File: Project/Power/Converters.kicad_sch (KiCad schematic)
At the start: 7 parts, among them U1 AP63203WU

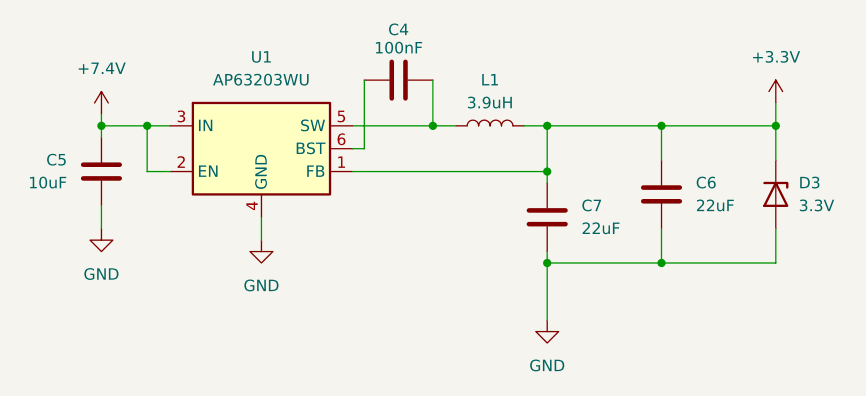
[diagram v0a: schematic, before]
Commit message: Add high-side power switch with LM74502
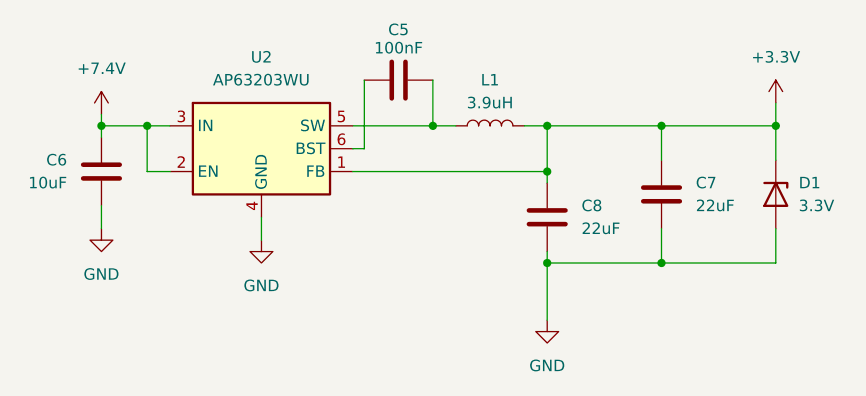
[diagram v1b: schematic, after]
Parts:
- renumbered C4 to C5, C5 to C6, C6 to C7, C7 to C8, D3 to D1, U1 to U2
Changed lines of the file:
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@@
 		(on_board yes)
 		(dnp no)
-		(property "Reference" "C6"
+		(property "Reference" "C7"
 			(at 116.84 44.4499 0)
 			(effects
@@
 			(project "XuLabPower"
 				(path "/71bb14ae-b730-4d22-a41d-cf68989dae2d/39e94aee-ccd8-45cb-a26b-136997d4dd4d"
-					(reference "C6")
+					(reference "C7")
 					(unit 1)
 				)
@@
 		(dnp no)
 		(fields_autoplaced yes)
-		(property "Reference" "#PWR05"
+		(property "Reference" "#PWR09"
 			(at 125.73 39.37 0)
 			(effects
@@
 			(project "XuLabPower"
 				(path "/71bb14ae-b730-4d22-a41d-cf68989dae2d/39e94aee-ccd8-45cb-a26b-136997d4dd4d"
-					(reference "#PWR05")
+					(reference "#PWR09")
 					(unit 1)
 				)
@@
 		(dnp no)
 		(fields_autoplaced yes)
-		(property "Reference" "U1"
+		(property "Reference" "U2"
 			(at 68.58 30.48 0)
 			(effects
@@
 			(project "XuLabPower"
 				(path "/71bb14ae-b730-4d22-a41d-cf68989dae2d/39e94aee-ccd8-45cb-a26b-136997d4dd4d"
-					(reference "U1")
+					(reference "U2")
 					(unit 1)
 				)
@@
 		(dnp no)
 		(fields_autoplaced yes)
-		(property "Reference" "#PWR07"
+		(property "Reference" "#PWR011"
 			(at 50.8 55.88 0)
 			(effects
@@
 			(project "XuLabPower"
 				(path "/71bb14ae-b730-4d22-a41d-cf68989dae2d/39e94aee-ccd8-45cb-a26b-136997d4dd4d"
-					(reference "#PWR07")
+					(reference "#PWR011")
 					(unit 1)
 				)
@@
 		(dnp no)
 		(fields_autoplaced yes)
-		(property "Reference" "#PWR09"
+		(property "Reference" "#PWR013"
 			(at 100.33 66.04 0)
 			(effects
@@
 			(project "XuLabPower"
 				(path "/71bb14ae-b730-4d22-a41d-cf68989dae2d/39e94aee-ccd8-45cb-a26b-136997d4dd4d"
-					(reference "#PWR09")
+					(reference "#PWR013")
 					(unit 1)
 				)
@@
 		(on_board yes)
 		(dnp no)
-		(property "Reference" "C5"
+		(property "Reference" "C6"
 			(at 46.99 41.9099 0)
 			(effects
@@
 			(project "XuLabPower"
 				(path "/71bb14ae-b730-4d22-a41d-cf68989dae2d/39e94aee-ccd8-45cb-a26b-136997d4dd4d"
-					(reference "C5")
+					(reference "C6")
 					(unit 1)
 				)
@@
 		(on_board yes)
 		(dnp no)
-		(property "Reference" "C4"
+		(property "Reference" "C5"
 			(at 83.82 27.432 90)
 			(effects
@@
 			(project "XuLabPower"
 				(path "/71bb14ae-b730-4d22-a41d-cf68989dae2d/39e94aee-ccd8-45cb-a26b-136997d4dd4d"
-					(reference "C4")
+					(reference "C5")
 					(unit 1)
 				)
@@
 		(dnp no)
 		(fields_autoplaced yes)
-		(property "Reference" "D3"
+		(property "Reference" "D1"
 			(at 128.27 44.4499 90)
 			(effects
@@
 			(project "XuLabPower"
 				(path "/71bb14ae-b730-4d22-a41d-cf68989dae2d/39e94aee-ccd8-45cb-a26b-136997d4dd4d"
-					(reference "D3")
+					(reference "D1")
 					(unit 1)
 				)
@@
 		(dnp no)
 		(fields_autoplaced yes)
-		(property "Reference" "#PWR06"
+		(property "Reference" "#PWR010"
 			(at 50.8 40.64 0)
 			(effects
@@
 			(project "XuLabPower"
 				(path "/71bb14ae-b730-4d22-a41d-cf68989dae2d/39e94aee-ccd8-45cb-a26b-136997d4dd4d"
-					(reference "#PWR06")
+					(reference "#PWR010")
 					(unit 1)
 				)
@@
 		(dnp no)
 		(fields_autoplaced yes)
-		(property "Reference" "#PWR08"
+		(property "Reference" "#PWR012"
 			(at 68.58 57.15 0)
 			(effects
@@
 			(project "XuLabPower"
 				(path "/71bb14ae-b730-4d22-a41d-cf68989dae2d/39e94aee-ccd8-45cb-a26b-136997d4dd4d"
-					(reference "#PWR08")
+					(reference "#PWR012")
 					(unit 1)
 				)
@@
 		(on_board yes)
 		(dnp no)
-		(property "Reference" "C7"
+		(property "Reference" "C8"
 			(at 104.14 46.9899 0)
 			(effects
@@
 			(project "XuLabPower"
 				(path "/71bb14ae-b730-4d22-a41d-cf68989dae2d/39e94aee-ccd8-45cb-a26b-136997d4dd4d"
-					(reference "C7")
-					(unit 1)
-				)
+					(reference "C8")
+					(unit 1)
+				)

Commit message: Add indicator LEDs to the batteries
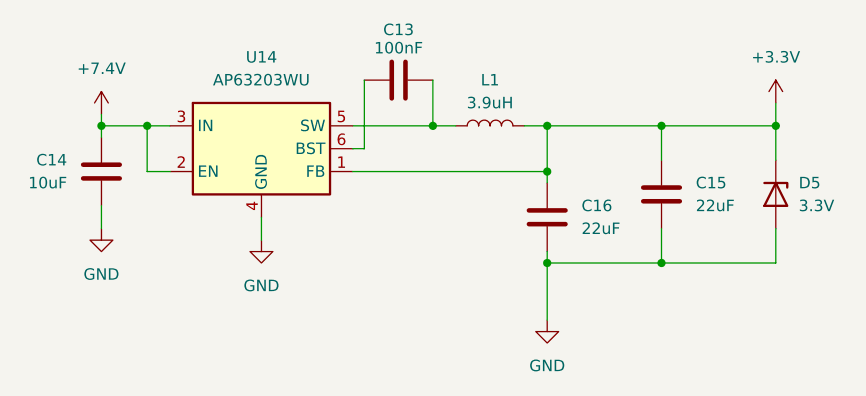
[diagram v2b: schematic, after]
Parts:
- renumbered C5 to C13, C6 to C14, C7 to C15, C8 to C16, D1 to D5, U2 to U14
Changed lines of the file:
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@@
 		(on_board yes)
 		(dnp no)
-		(property "Reference" "C7"
+		(property "Reference" "C15"
 			(at 116.84 44.4499 0)
 			(effects
@@
 			(project "XuLabPower"
 				(path "/71bb14ae-b730-4d22-a41d-cf68989dae2d/39e94aee-ccd8-45cb-a26b-136997d4dd4d"
-					(reference "C7")
+					(reference "C15")
 					(unit 1)
 				)
@@
 		(dnp no)
 		(fields_autoplaced yes)
-		(property "Reference" "#PWR09"
+		(property "Reference" "#PWR060"
 			(at 125.73 39.37 0)
 			(effects
@@
 			(project "XuLabPower"
 				(path "/71bb14ae-b730-4d22-a41d-cf68989dae2d/39e94aee-ccd8-45cb-a26b-136997d4dd4d"
-					(reference "#PWR09")
+					(reference "#PWR060")
 					(unit 1)
 				)
@@
 		(dnp no)
 		(fields_autoplaced yes)
-		(property "Reference" "U2"
+		(property "Reference" "U14"
 			(at 68.58 30.48 0)
 			(effects
@@
 			(project "XuLabPower"
 				(path "/71bb14ae-b730-4d22-a41d-cf68989dae2d/39e94aee-ccd8-45cb-a26b-136997d4dd4d"
-					(reference "U2")
+					(reference "U14")
 					(unit 1)
 				)
@@
 		(dnp no)
 		(fields_autoplaced yes)
-		(property "Reference" "#PWR011"
+		(property "Reference" "#PWR062"
 			(at 50.8 55.88 0)
 			(effects
@@
 			(project "XuLabPower"
 				(path "/71bb14ae-b730-4d22-a41d-cf68989dae2d/39e94aee-ccd8-45cb-a26b-136997d4dd4d"
-					(reference "#PWR011")
+					(reference "#PWR062")
 					(unit 1)
 				)
@@
 		(dnp no)
 		(fields_autoplaced yes)
-		(property "Reference" "#PWR013"
+		(property "Reference" "#PWR064"
 			(at 100.33 66.04 0)
 			(effects
@@
 			(project "XuLabPower"
 				(path "/71bb14ae-b730-4d22-a41d-cf68989dae2d/39e94aee-ccd8-45cb-a26b-136997d4dd4d"
-					(reference "#PWR013")
+					(reference "#PWR064")
 					(unit 1)
 				)
@@
 		(on_board yes)
 		(dnp no)
-		(property "Reference" "C6"
+		(property "Reference" "C14"
 			(at 46.99 41.9099 0)
 			(effects
@@
 			(project "XuLabPower"
 				(path "/71bb14ae-b730-4d22-a41d-cf68989dae2d/39e94aee-ccd8-45cb-a26b-136997d4dd4d"
-					(reference "C6")
+					(reference "C14")
 					(unit 1)
 				)
@@
 		(on_board yes)
 		(dnp no)
-		(property "Reference" "C5"
+		(property "Reference" "C13"
 			(at 83.82 27.432 90)
 			(effects
@@
 			(project "XuLabPower"
 				(path "/71bb14ae-b730-4d22-a41d-cf68989dae2d/39e94aee-ccd8-45cb-a26b-136997d4dd4d"
-					(reference "C5")
+					(reference "C13")
 					(unit 1)
 				)
@@
 		(dnp no)
 		(fields_autoplaced yes)
-		(property "Reference" "D1"
+		(property "Reference" "D5"
 			(at 128.27 44.4499 90)
 			(effects
@@
 			(project "XuLabPower"
 				(path "/71bb14ae-b730-4d22-a41d-cf68989dae2d/39e94aee-ccd8-45cb-a26b-136997d4dd4d"
-					(reference "D1")
+					(reference "D5")
 					(unit 1)
 				)
@@
 		(dnp no)
 		(fields_autoplaced yes)
-		(property "Reference" "#PWR010"
+		(property "Reference" "#PWR061"
 			(at 50.8 40.64 0)
 			(effects
@@
 			(project "XuLabPower"
 				(path "/71bb14ae-b730-4d22-a41d-cf68989dae2d/39e94aee-ccd8-45cb-a26b-136997d4dd4d"
-					(reference "#PWR010")
+					(reference "#PWR061")
 					(unit 1)
 				)
@@
 		(dnp no)
 		(fields_autoplaced yes)
-		(property "Reference" "#PWR012"
+		(property "Reference" "#PWR063"
 			(at 68.58 57.15 0)
 			(effects
@@
 			(project "XuLabPower"
 				(path "/71bb14ae-b730-4d22-a41d-cf68989dae2d/39e94aee-ccd8-45cb-a26b-136997d4dd4d"
-					(reference "#PWR012")
+					(reference "#PWR063")
 					(unit 1)
 				)
@@
 		(on_board yes)
 		(dnp no)
-		(property "Reference" "C8"
+		(property "Reference" "C16"
 			(at 104.14 46.9899 0)
 			(effects
@@
 			(project "XuLabPower"
 				(path "/71bb14ae-b730-4d22-a41d-cf68989dae2d/39e94aee-ccd8-45cb-a26b-136997d4dd4d"
-					(reference "C8")
-					(unit 1)
-				)
+					(reference "C16")
+					(unit 1)
+				)

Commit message: Add STM32L422KBTx microcontroller
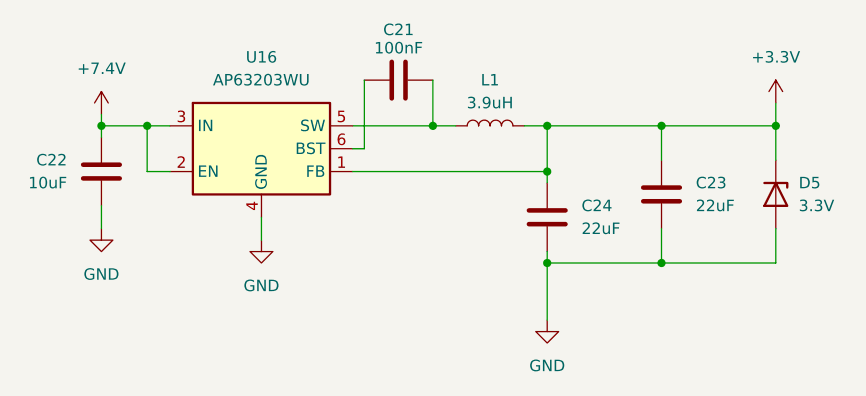
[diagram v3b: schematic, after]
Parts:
- renumbered C13 to C21, C14 to C22, C15 to C23, C16 to C24, U14 to U16
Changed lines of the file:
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@@
 		(on_board yes)
 		(dnp no)
-		(property "Reference" "C15"
+		(property "Reference" "C23"
 			(at 116.84 44.4499 0)
 			(effects
@@
 			(project "XuLabPower"
 				(path "/71bb14ae-b730-4d22-a41d-cf68989dae2d/39e94aee-ccd8-45cb-a26b-136997d4dd4d"
-					(reference "C15")
+					(reference "C23")
 					(unit 1)
 				)
@@
 		(dnp no)
 		(fields_autoplaced yes)
-		(property "Reference" "#PWR060"
+		(property "Reference" "#PWR076"
 			(at 125.73 39.37 0)
 			(effects
@@
 			(project "XuLabPower"
 				(path "/71bb14ae-b730-4d22-a41d-cf68989dae2d/39e94aee-ccd8-45cb-a26b-136997d4dd4d"
-					(reference "#PWR060")
+					(reference "#PWR076")
 					(unit 1)
 				)
@@
 		(dnp no)
 		(fields_autoplaced yes)
-		(property "Reference" "U14"
+		(property "Reference" "U16"
 			(at 68.58 30.48 0)
 			(effects
@@
 			(project "XuLabPower"
 				(path "/71bb14ae-b730-4d22-a41d-cf68989dae2d/39e94aee-ccd8-45cb-a26b-136997d4dd4d"
-					(reference "U14")
+					(reference "U16")
 					(unit 1)
 				)
@@
 		(dnp no)
 		(fields_autoplaced yes)
-		(property "Reference" "#PWR062"
+		(property "Reference" "#PWR078"
 			(at 50.8 55.88 0)
 			(effects
@@
 			(project "XuLabPower"
 				(path "/71bb14ae-b730-4d22-a41d-cf68989dae2d/39e94aee-ccd8-45cb-a26b-136997d4dd4d"
-					(reference "#PWR062")
+					(reference "#PWR078")
 					(unit 1)
 				)
@@
 		(dnp no)
 		(fields_autoplaced yes)
-		(property "Reference" "#PWR064"
+		(property "Reference" "#PWR080"
 			(at 100.33 66.04 0)
 			(effects
@@
 			(project "XuLabPower"
 				(path "/71bb14ae-b730-4d22-a41d-cf68989dae2d/39e94aee-ccd8-45cb-a26b-136997d4dd4d"
-					(reference "#PWR064")
+					(reference "#PWR080")
 					(unit 1)
 				)
@@
 		(on_board yes)
 		(dnp no)
-		(property "Reference" "C14"
+		(property "Reference" "C22"
 			(at 46.99 41.9099 0)
 			(effects
@@
 			(project "XuLabPower"
 				(path "/71bb14ae-b730-4d22-a41d-cf68989dae2d/39e94aee-ccd8-45cb-a26b-136997d4dd4d"
-					(reference "C14")
+					(reference "C22")
 					(unit 1)
 				)
@@
 		(on_board yes)
 		(dnp no)
-		(property "Reference" "C13"
+		(property "Reference" "C21"
 			(at 83.82 27.432 90)
 			(effects
@@
 			(project "XuLabPower"
 				(path "/71bb14ae-b730-4d22-a41d-cf68989dae2d/39e94aee-ccd8-45cb-a26b-136997d4dd4d"
-					(reference "C13")
+					(reference "C21")
 					(unit 1)
 				)
@@
 		(dnp no)
 		(fields_autoplaced yes)
-		(property "Reference" "#PWR061"
+		(property "Reference" "#PWR077"
 			(at 50.8 40.64 0)
 			(effects
@@
 			(project "XuLabPower"
 				(path "/71bb14ae-b730-4d22-a41d-cf68989dae2d/39e94aee-ccd8-45cb-a26b-136997d4dd4d"
-					(reference "#PWR061")
+					(reference "#PWR077")
 					(unit 1)
 				)
@@
 		(dnp no)
 		(fields_autoplaced yes)
-		(property "Reference" "#PWR063"
+		(property "Reference" "#PWR079"
 			(at 68.58 57.15 0)
 			(effects
@@
 			(project "XuLabPower"
 				(path "/71bb14ae-b730-4d22-a41d-cf68989dae2d/39e94aee-ccd8-45cb-a26b-136997d4dd4d"
-					(reference "#PWR063")
+					(reference "#PWR079")
 					(unit 1)
 				)
@@
 		(on_board yes)
 		(dnp no)
-		(property "Reference" "C16"
+		(property "Reference" "C24"
 			(at 104.14 46.9899 0)
 			(effects
@@
 			(project "XuLabPower"
 				(path "/71bb14ae-b730-4d22-a41d-cf68989dae2d/39e94aee-ccd8-45cb-a26b-136997d4dd4d"
-					(reference "C16")
-					(unit 1)
-				)
+					(reference "C24")
+					(unit 1)
+				)

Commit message: Make microcontroller always-on
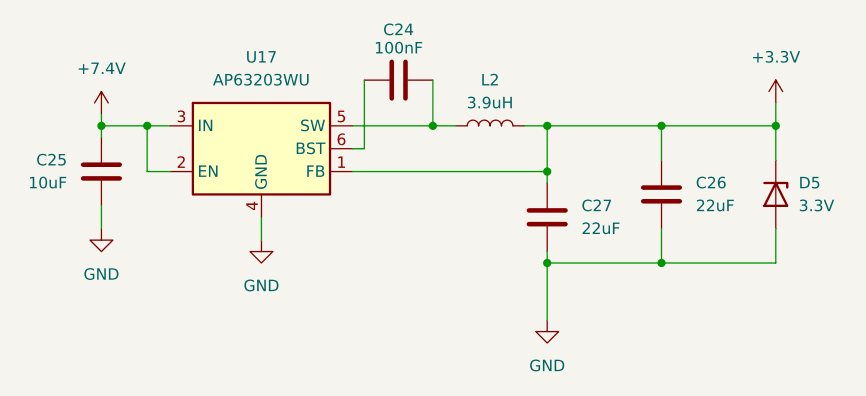
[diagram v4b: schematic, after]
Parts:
- renumbered C21 to C24, C22 to C25, C23 to C26, C24 to C27, L1 to L2, U16 to U17
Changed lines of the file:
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@@
 		(on_board yes)
 		(dnp no)
-		(property "Reference" "C23"
+		(property "Reference" "C26"
 			(at 116.84 44.4499 0)
 			(effects
@@
 			(project "XuLabPower"
 				(path "/71bb14ae-b730-4d22-a41d-cf68989dae2d/39e94aee-ccd8-45cb-a26b-136997d4dd4d"
-					(reference "C23")
+					(reference "C26")
 					(unit 1)
 				)
@@
 		(dnp no)
 		(fields_autoplaced yes)
-		(property "Reference" "#PWR076"
+		(property "Reference" "#PWR078"
 			(at 125.73 39.37 0)
 			(effects
@@
 			(project "XuLabPower"
 				(path "/71bb14ae-b730-4d22-a41d-cf68989dae2d/39e94aee-ccd8-45cb-a26b-136997d4dd4d"
-					(reference "#PWR076")
+					(reference "#PWR078")
 					(unit 1)
 				)
@@
 		(dnp no)
 		(fields_autoplaced yes)
-		(property "Reference" "U16"
+		(property "Reference" "U17"
 			(at 68.58 30.48 0)
 			(effects
@@
 			(project "XuLabPower"
 				(path "/71bb14ae-b730-4d22-a41d-cf68989dae2d/39e94aee-ccd8-45cb-a26b-136997d4dd4d"
-					(reference "U16")
+					(reference "U17")
 					(unit 1)
 				)
@@
 		(dnp no)
 		(fields_autoplaced yes)
-		(property "Reference" "#PWR078"
+		(property "Reference" "#PWR080"
 			(at 50.8 55.88 0)
 			(effects
@@
 			(project "XuLabPower"
 				(path "/71bb14ae-b730-4d22-a41d-cf68989dae2d/39e94aee-ccd8-45cb-a26b-136997d4dd4d"
-					(reference "#PWR078")
+					(reference "#PWR080")
 					(unit 1)
 				)
@@
 		(dnp no)
 		(fields_autoplaced yes)
-		(property "Reference" "#PWR080"
+		(property "Reference" "#PWR082"
 			(at 100.33 66.04 0)
 			(effects
@@
 			(project "XuLabPower"
 				(path "/71bb14ae-b730-4d22-a41d-cf68989dae2d/39e94aee-ccd8-45cb-a26b-136997d4dd4d"
-					(reference "#PWR080")
+					(reference "#PWR082")
 					(unit 1)
 				)
@@
 		(on_board yes)
 		(dnp no)
-		(property "Reference" "C22"
+		(property "Reference" "C25"
 			(at 46.99 41.9099 0)
 			(effects
@@
 			(project "XuLabPower"
 				(path "/71bb14ae-b730-4d22-a41d-cf68989dae2d/39e94aee-ccd8-45cb-a26b-136997d4dd4d"
-					(reference "C22")
+					(reference "C25")
 					(unit 1)
 				)
@@
 		(on_board yes)
 		(dnp no)
-		(property "Reference" "C21"
+		(property "Reference" "C24"
 			(at 83.82 27.432 90)
 			(effects
@@
 			(project "XuLabPower"
 				(path "/71bb14ae-b730-4d22-a41d-cf68989dae2d/39e94aee-ccd8-45cb-a26b-136997d4dd4d"
-					(reference "C21")
+					(reference "C24")
 					(unit 1)
 				)
@@
 		(dnp no)
 		(fields_autoplaced yes)
-		(property "Reference" "#PWR077"
+		(property "Reference" "#PWR079"
 			(at 50.8 40.64 0)
 			(effects
@@
 			(project "XuLabPower"
 				(path "/71bb14ae-b730-4d22-a41d-cf68989dae2d/39e94aee-ccd8-45cb-a26b-136997d4dd4d"
-					(reference "#PWR077")
+					(reference "#PWR079")
 					(unit 1)
 				)
@@
 		(dnp no)
 		(fields_autoplaced yes)
-		(property "Reference" "L1"
+		(property "Reference" "L2"
 			(at 93.98 33.02 90)
 			(effects
@@
 			(project "XuLabPower"
 				(path "/71bb14ae-b730-4d22-a41d-cf68989dae2d/39e94aee-ccd8-45cb-a26b-136997d4dd4d"
-					(reference "L1")
+					(reference "L2")
 					(unit 1)
 				)
@@
 		(dnp no)
 		(fields_autoplaced yes)
-		(property "Reference" "#PWR079"
+		(property "Reference" "#PWR081"
 			(at 68.58 57.15 0)
 			(effects
@@
 			(project "XuLabPower"
 				(path "/71bb14ae-b730-4d22-a41d-cf68989dae2d/39e94aee-ccd8-45cb-a26b-136997d4dd4d"
-					(reference "#PWR079")
+					(reference "#PWR081")
 					(unit 1)
 				)
@@
 		(on_board yes)
 		(dnp no)
-		(property "Reference" "C24"
+		(property "Reference" "C27"
 			(at 104.14 46.9899 0)
 			(effects
@@
 			(project "XuLabPower"
 				(path "/71bb14ae-b730-4d22-a41d-cf68989dae2d/39e94aee-ccd8-45cb-a26b-136997d4dd4d"
-					(reference "C24")
-					(unit 1)
-				)
+					(reference "C27")
+					(unit 1)
+				)

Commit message: Add SPI and I2C connectors for microcontroller
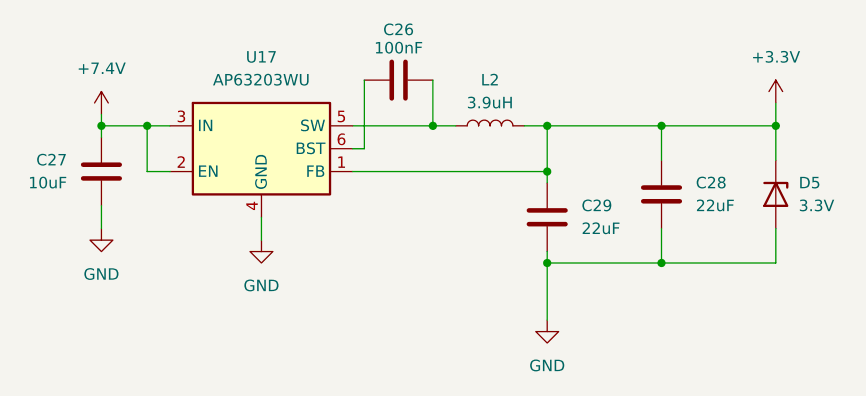
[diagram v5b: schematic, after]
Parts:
- renumbered C24 to C26, C25 to C27, C26 to C28, C27 to C29
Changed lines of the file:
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@@
 		(on_board yes)
 		(dnp no)
-		(property "Reference" "C26"
+		(property "Reference" "C28"
 			(at 116.84 44.4499 0)
 			(effects
@@
 			(project "XuLabPower"
 				(path "/71bb14ae-b730-4d22-a41d-cf68989dae2d/39e94aee-ccd8-45cb-a26b-136997d4dd4d"
-					(reference "C26")
+					(reference "C28")
 					(unit 1)
 				)
@@
 		(dnp no)
 		(fields_autoplaced yes)
-		(property "Reference" "#PWR078"
+		(property "Reference" "#PWR086"
 			(at 125.73 39.37 0)
 			(effects
@@
 			(project "XuLabPower"
 				(path "/71bb14ae-b730-4d22-a41d-cf68989dae2d/39e94aee-ccd8-45cb-a26b-136997d4dd4d"
-					(reference "#PWR078")
+					(reference "#PWR086")
 					(unit 1)
 				)
@@
 		(dnp no)
 		(fields_autoplaced yes)
-		(property "Reference" "#PWR080"
+		(property "Reference" "#PWR088"
 			(at 50.8 55.88 0)
 			(effects
@@
 			(project "XuLabPower"
 				(path "/71bb14ae-b730-4d22-a41d-cf68989dae2d/39e94aee-ccd8-45cb-a26b-136997d4dd4d"
-					(reference "#PWR080")
+					(reference "#PWR088")
 					(unit 1)
 				)
@@
 		(dnp no)
 		(fields_autoplaced yes)
-		(property "Reference" "#PWR082"
+		(property "Reference" "#PWR090"
 			(at 100.33 66.04 0)
 			(effects
@@
 			(project "XuLabPower"
 				(path "/71bb14ae-b730-4d22-a41d-cf68989dae2d/39e94aee-ccd8-45cb-a26b-136997d4dd4d"
-					(reference "#PWR082")
+					(reference "#PWR090")
 					(unit 1)
 				)
@@
 		(on_board yes)
 		(dnp no)
-		(property "Reference" "C25"
+		(property "Reference" "C27"
 			(at 46.99 41.9099 0)
 			(effects
@@
 			(project "XuLabPower"
 				(path "/71bb14ae-b730-4d22-a41d-cf68989dae2d/39e94aee-ccd8-45cb-a26b-136997d4dd4d"
-					(reference "C25")
+					(reference "C27")
 					(unit 1)
 				)
@@
 		(on_board yes)
 		(dnp no)
-		(property "Reference" "C24"
+		(property "Reference" "C26"
 			(at 83.82 27.432 90)
 			(effects
@@
 			(project "XuLabPower"
 				(path "/71bb14ae-b730-4d22-a41d-cf68989dae2d/39e94aee-ccd8-45cb-a26b-136997d4dd4d"
-					(reference "C24")
+					(reference "C26")
 					(unit 1)
 				)
@@
 		(dnp no)
 		(fields_autoplaced yes)
-		(property "Reference" "#PWR079"
+		(property "Reference" "#PWR087"
 			(at 50.8 40.64 0)
 			(effects
@@
 			(project "XuLabPower"
 				(path "/71bb14ae-b730-4d22-a41d-cf68989dae2d/39e94aee-ccd8-45cb-a26b-136997d4dd4d"
-					(reference "#PWR079")
+					(reference "#PWR087")
 					(unit 1)
 				)
@@
 		(dnp no)
 		(fields_autoplaced yes)
-		(property "Reference" "#PWR081"
+		(property "Reference" "#PWR089"
 			(at 68.58 57.15 0)
 			(effects
@@
 			(project "XuLabPower"
 				(path "/71bb14ae-b730-4d22-a41d-cf68989dae2d/39e94aee-ccd8-45cb-a26b-136997d4dd4d"
-					(reference "#PWR081")
+					(reference "#PWR089")
 					(unit 1)
 				)
@@
 		(on_board yes)
 		(dnp no)
-		(property "Reference" "C27"
+		(property "Reference" "C29"
 			(at 104.14 46.9899 0)
 			(effects
@@
 			(project "XuLabPower"
 				(path "/71bb14ae-b730-4d22-a41d-cf68989dae2d/39e94aee-ccd8-45cb-a26b-136997d4dd4d"
-					(reference "C27")
-					(unit 1)
-				)
+					(reference "C29")
+					(unit 1)
+				)
